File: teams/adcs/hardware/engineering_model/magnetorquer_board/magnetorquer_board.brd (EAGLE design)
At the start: 90 x 90 mm, 36 parts

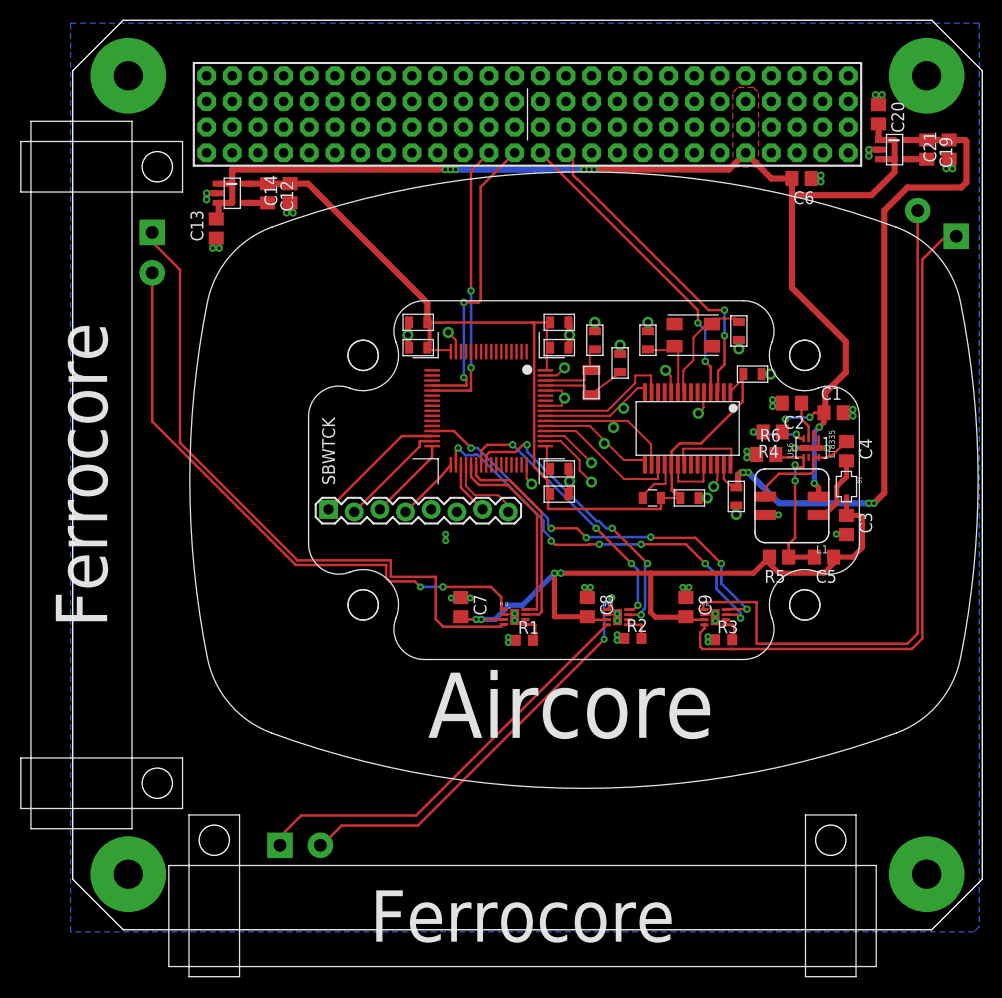
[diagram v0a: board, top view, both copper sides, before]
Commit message: added two new capacitors to eagle library moved estimator, photodiode_center, and magetorquer board to their own foldr and created gerbers for them
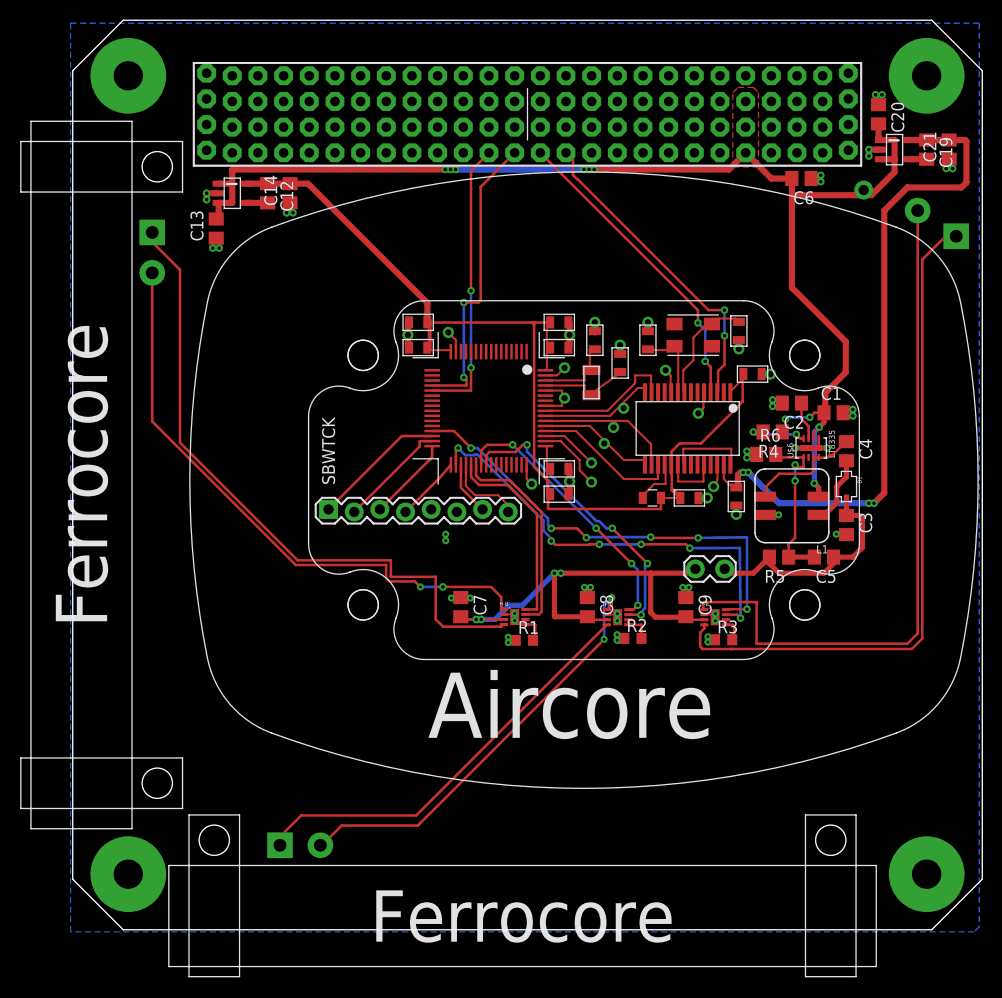
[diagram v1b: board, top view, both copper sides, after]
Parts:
- added JP1: M02LOCK, SparkFun-Connectors:1X02_LOCK
- added JP2: M01NOSILK-KIT, SparkFun-Connectors:1X01NS-KIT
- U$2: value BOARD_TEMPLATE -> BOARD_TEMPLATE1
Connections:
- net 6V: now also JP1.1, JP1.2
- net VBAT: now also JP2.1
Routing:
- net PWM_Z_2: track 42.2 -> 45.2 mm
- net PWM_Z_1: track 40.2 -> 43.1 mm
- net 6V: track 73.3 -> 71.3 mm
